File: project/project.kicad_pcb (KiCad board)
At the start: 4 copper layers, 84 x 84 mm, 163 parts, among them J101 BUS, J102 BUS, J103 FFC, J104 Back, J105 Front, J301 5V, J302 24V, J303 3V3, J401 USB_C_Receptacle_USB2.0, SW101 SW_DIP_x04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

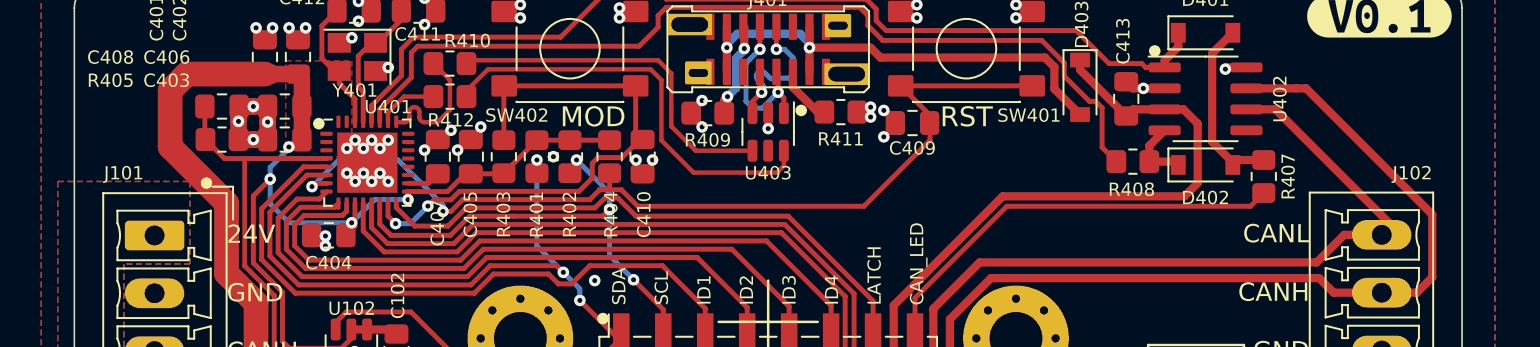
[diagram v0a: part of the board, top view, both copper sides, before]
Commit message: adding some 3d models
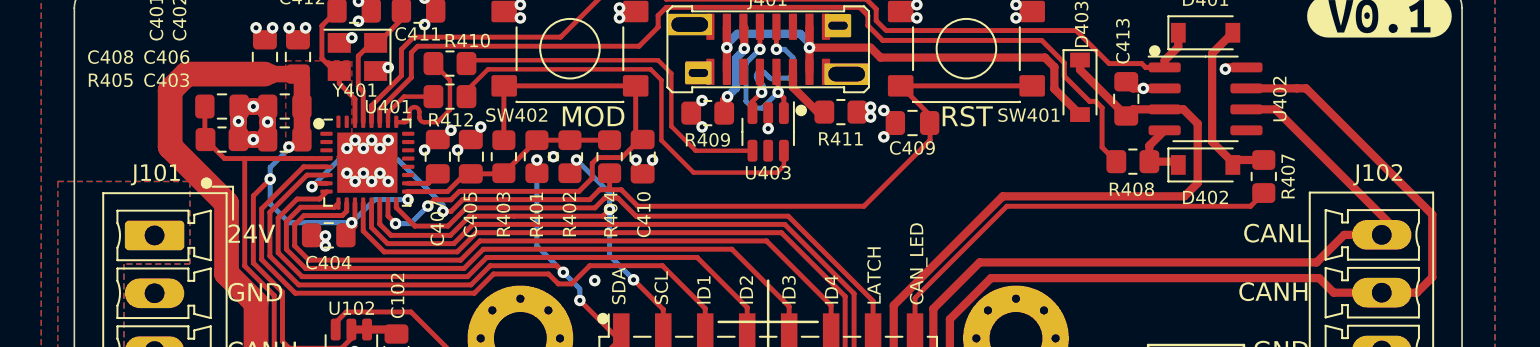
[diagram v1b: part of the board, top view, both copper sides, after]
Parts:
- J101, J102: footprint Connector_Phoenix_MC:PhoenixContact_MCV_1,5_4-G-3.5_1x04_P3.50mm_Vertical -> -local:PhoenixContact_MCV_1,5_4-G-3.5_1x04_P3.50mm_Vertical
